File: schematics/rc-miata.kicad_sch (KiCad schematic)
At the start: 14 parts, among them M1 BLDC_MOTOR, M2 22KG SERVO, U2 UBEC, U3 ESC, U4 ESP32 DEVKITV1

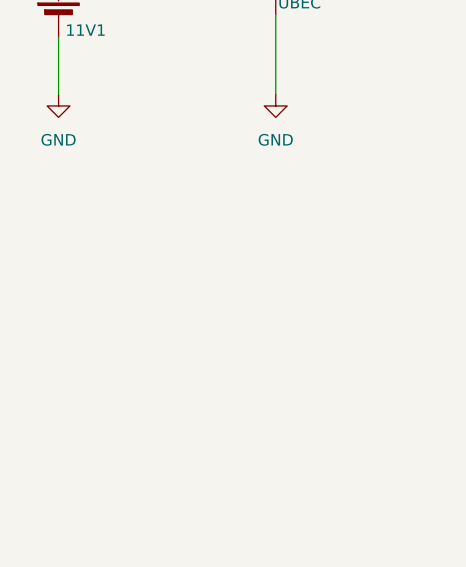
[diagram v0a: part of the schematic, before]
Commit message: Finished 2,3, and 4 Terminal Blocks Added Battery Terminal
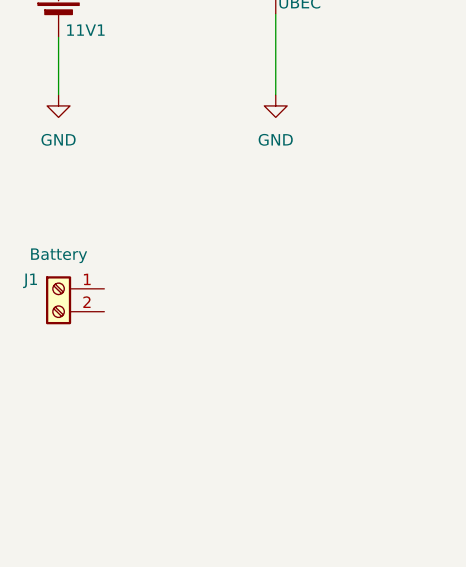
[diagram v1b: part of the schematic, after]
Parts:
- added J1: Battery, symbol Connectors:2 Screw Terminal
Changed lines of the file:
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@@
+	)
+	(symbol
+		(lib_id "Connectors:2 Screw Terminal")
+		(at 38.1 105.41 0)
+		(unit 1)
+		(body_style 1)
+		(exclude_from_sim no)
+		(in_bom yes)
+		(on_board yes)
+		(in_pos_files yes)
+		(dnp no)
+		(property "Reference" "J1"
+			(at 36.322 105.664 0)
+			(show_name no)
+			(do_not_autoplace no)
+			(effects
+				(font
+					(size 1.27 1.27)
+				)
+			)
+		)
+		(property "Value" "Battery"
+			(at 39.37 102.87 0)
+			(show_name no)
+			(do_not_autoplace no)
+			(effects
+				(font
+					(size 1.27 1.27)
+				)
+			)
+		)
+		(property "Footprint" ""
+			(at 38.1 105.41 0)
+			(hide yes)
+			(show_name no)
+			(do_not_autoplace no)
+			(effects
+				(font
+					(size 1.27 1.27)
+				)
+			)
+		)
+		(property "Datasheet" "https://www.mouser.ca/datasheet/3/507/9/phoenix_contact_1869211_en.pdf"
+			(at 59.944 127.508 0)
+			(hide yes)
+			(show_name no)
+			(do_not_autoplace no)
+			(effects
+				(font
+					(size 1.27 1.27)
+				)
+			)
+		)
+		(property "Description" "Phoenix Contact screw terminal, single row, 01x02"
+			(at 63.246 122.428 0)
+			(hide yes)
+			(show_name no)
+			(do_not_autoplace no)
+			(effects
+				(font
+					(size 1.27 1.27)
+				)
+			)
+		)
+		(property "Mfr. #" "1869211"
+			(at 42.418 119.888 0)
+			(hide yes)
+			(show_name no)
+			(do_not_autoplace no)
+			(effects
+				(font
+					(size 1.27 1.27)
+				)
+			)
+		)
+		(property "Mfr." "Phoenix Contact"
+			(at 46.228 124.46 0)
+			(hide yes)
+			(show_name no)
+			(do_not_autoplace no)
+			(effects
+				(font
+					(size 1.27 1.27)
+				)
+			)
+		)
+		(property "Mouser #" "651-1869211"
+			(at 45.72 130.556 0)
+			(hide yes)
+			(show_name no)
+			(do_not_autoplace no)
+			(effects
+				(font
+					(size 1.27 1.27)
+				)
+			)
+		)
+		(pin "1"
+		)
+		(pin "2"
+		)
+		(instances
+			(project "rc-miata"
+				(path "/59cbdaad-7c89-4958-b9bb-08b035442600"
+					(reference "J1")
+					(unit 1)
+				)
+			)
+		)
 	)
 	(symbol

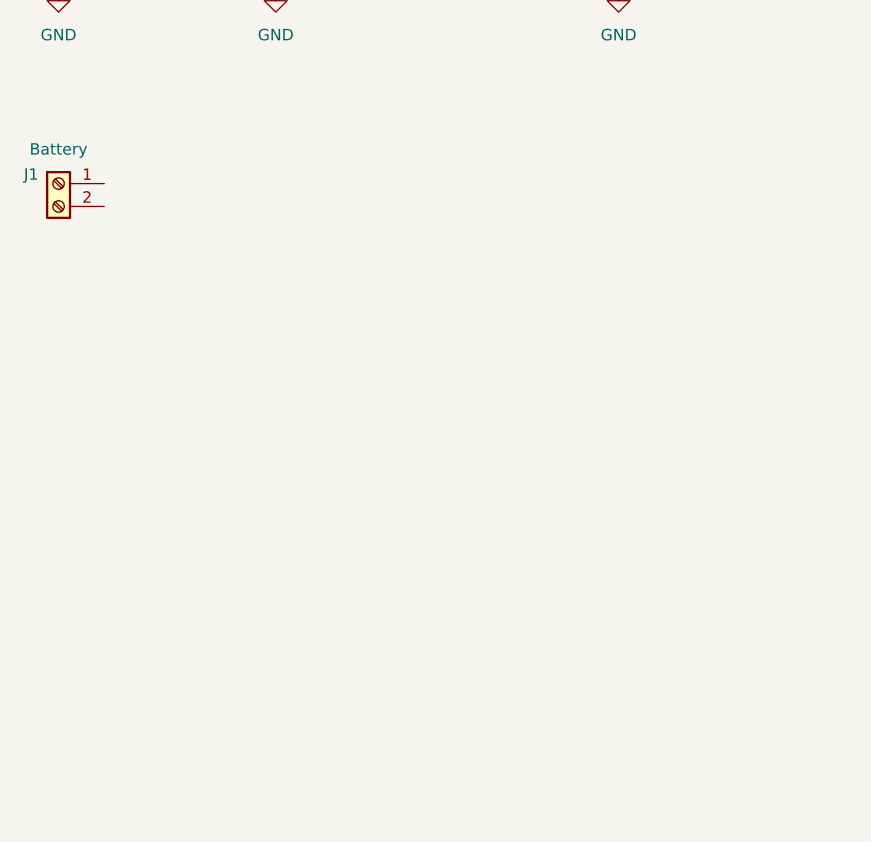
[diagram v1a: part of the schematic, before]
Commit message: Added and wired terminal blocks to schematic
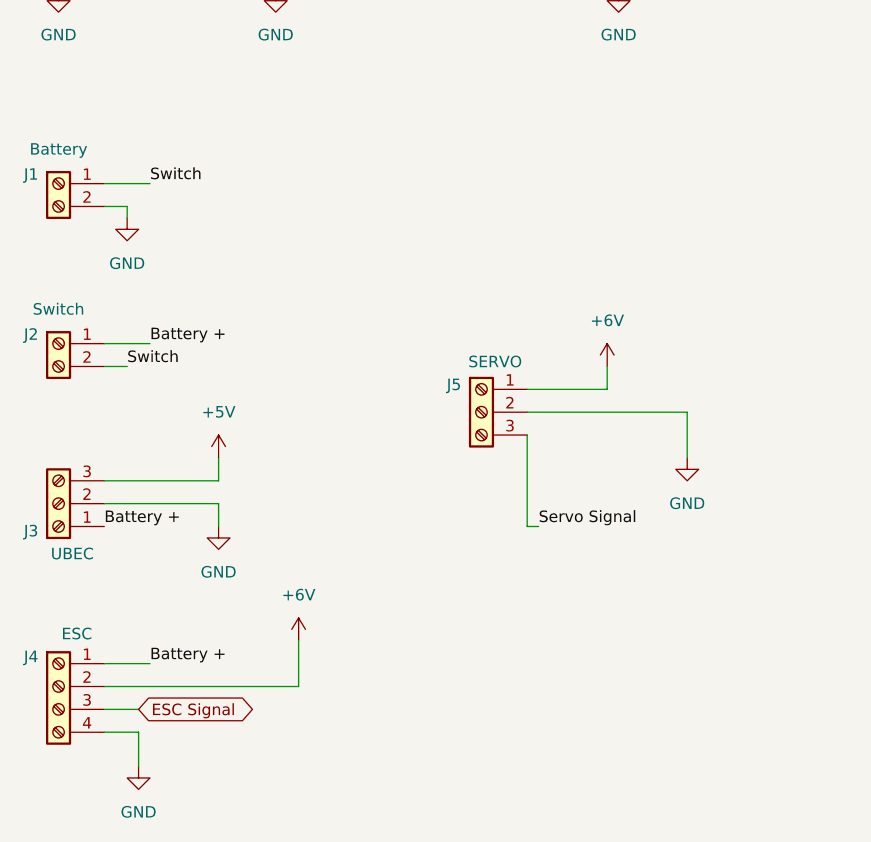
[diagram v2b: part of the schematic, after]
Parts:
- added J2: Switch, symbol Connectors:2 Screw Terminal
- added J3: UBEC, symbol Connectors:3 Screw Terminal
- added J4: ESC, symbol Connectors:4 Screw Terminal
- added J5: SERVO, symbol Connectors:3 Screw Terminal
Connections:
- net +5V: now also J3.3 (Pin_3)
- net +6V: now also J4.2 (Pin_2), J5.1 (Pin_1)
- net Battery +: now also J2.1 (Pin_1), J3.1 (Pin_1), J4.1 (Pin_1)
- net ESC Signal: now also J4.3 (Pin_3)
- net GND: now also J1.2 (Pin_2), J3.2 (Pin_2), J4.4 (Pin_4), J5.2 (Pin_2)
- net Servo Signal: now also J5.3 (Pin_3)
- net Switch: now also J1.1 (Pin_1), J2.2 (Pin_2)

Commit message: Fixed pin connections for servo and UBEC
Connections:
- net +5V: now also J3.1 (Pin_1); no longer J3.3 (Pin_3)
- net +6V: now also J5.3 (Pin_3); no longer J5.1 (Pin_1)
- net Battery +: now also J3.3 (Pin_3); no longer J3.1 (Pin_1)
- net Servo Signal: now also J5.1 (Pin_1); no longer J5.3 (Pin_3)
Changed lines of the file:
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@@
 	(symbol
 		(lib_id "Connectors:3 Screw Terminal")
-		(at 38.1 146.05 0)
-		(mirror x)
+		(at 38.1 138.43 0)
 		(unit 1)
 		(body_style 1)
@@
 		(dnp no)
 		(property "Reference" "J3"
-			(at 36.322 145.288 0)
+			(at 36.322 139.192 0)
 			(show_name no)
 			(do_not_autoplace no)
@@
 		)
 		(property "Value" "UBEC"
-			(at 40.894 147.828 0)
+			(at 40.894 136.652 0)
 			(show_name no)
 			(do_not_autoplace no)
@@
 		)
 		(property "Footprint" ""
-			(at 38.1 146.05 0)
+			(at 38.1 138.43 0)
 			(hide yes)
 			(show_name no)
@@
 		)
 		(property "Datasheet" "https://www.mouser.ca/datasheet/3/507/9/phoenix_contact_1161181_en.pdf"
-			(at 60.96 114.3 0)
+			(at 60.96 170.18 0)
 			(hide yes)
 			(show_name no)
@@
 		)
 		(property "Description" "Phoenix Contact screw terminal, single row, 01x03"
-			(at 63.246 129.032 0)
+			(at 63.246 155.448 0)
 			(hide yes)
 			(show_name no)
@@
 		)
 		(property "Mfr. #" "1161181"
-			(at 43.688 120.396 0)
+			(at 43.688 164.084 0)
 			(hide yes)
 			(show_name no)
@@
 		)
 		(property "Mfr." "Phoenix Contact"
-			(at 46.228 127 0)
+			(at 46.228 157.48 0)
 			(hide yes)
 			(show_name no)
@@
 		)
 		(property "Mouser #" "651-1161181"
-			(at 45.212 117.348 0)
+			(at 45.212 167.132 0)
 			(hide yes)
 			(show_name no)
@@
 		)
 		(property "Seller" "https://www.mouser.ca/ProductDetail/Phoenix-Contact/1161181?qs=sGAEpiMZZMvPvGwLNS671%252B7aWYNAXBhXqhzIwd5MSQGBxEXmvvVG1Q%3D%3D"
-			(at 60.452 110.744 0)
+			(at 60.452 173.736 0)
 			(hide yes)
 			(show_name no)
@@
 	(symbol
 		(lib_id "Connectors:3 Screw Terminal")
-		(at 85.09 128.27 0)
+		(at 85.09 135.89 0)
+		(mirror x)
 		(unit 1)
 		(body_style 1)
@@
 		(dnp no)
 		(property "Reference" "J5"
-			(at 83.312 129.032 0)
+			(at 83.312 135.128 0)
 			(show_name no)
 			(do_not_autoplace no)
@@
 		)
 		(property "Value" "SERVO"
-			(at 87.884 126.492 0)
+			(at 87.884 137.668 0)
 			(show_name no)
 			(do_not_autoplace no)
@@
 		)
 		(property "Footprint" ""
-			(at 85.09 128.27 0)
+			(at 85.09 135.89 0)
 			(hide yes)
 			(show_name no)
@@
 		)
 		(property "Datasheet" "https://www.mouser.ca/datasheet/3/507/9/phoenix_contact_1161181_en.pdf"
-			(at 107.95 160.02 0)
+			(at 107.95 104.14 0)
 			(hide yes)
 			(show_name no)
@@
 		)
 		(property "Description" "Phoenix Contact screw terminal, single row, 01x03"
-			(at 110.236 145.288 0)
+			(at 110.236 118.872 0)
 			(hide yes)
 			(show_name no)
@@
 		)
 		(property "Mfr. #" "1161181"
-			(at 90.678 153.924 0)
+			(at 90.678 110.236 0)
 			(hide yes)
 			(show_name no)
@@
 		)
 		(property "Mfr." "Phoenix Contact"
-			(at 93.218 147.32 0)
+			(at 93.218 116.84 0)
 			(hide yes)
 			(show_name no)
@@
 		)
 		(property "Mouser #" "651-1161181"
-			(at 92.202 156.972 0)
+			(at 92.202 107.188 0)
 			(hide yes)
 			(show_name no)
@@
 		)
 		(property "Seller" "https://www.mouser.ca/ProductDetail/Phoenix-Contact/1161181?qs=sGAEpiMZZMvPvGwLNS671%252B7aWYNAXBhXqhzIwd5MSQGBxEXmvvVG1Q%3D%3D"
-			(at 107.442 163.576 0)
+			(at 107.442 100.584 0)
 			(hide yes)
 			(show_name no)

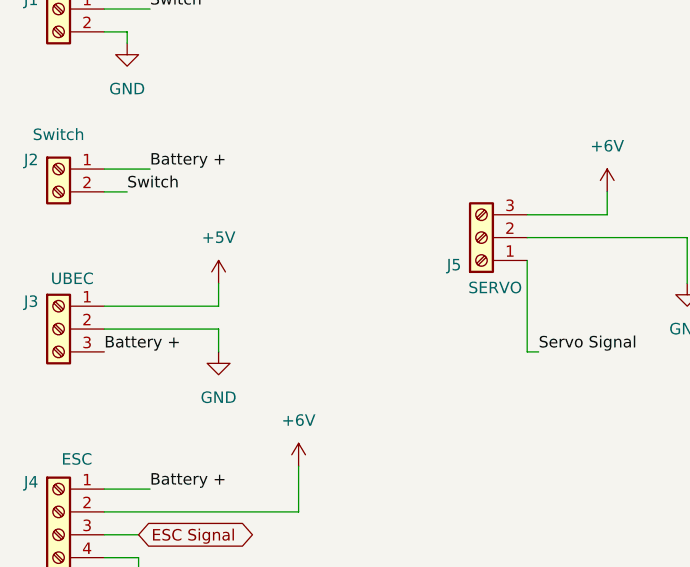
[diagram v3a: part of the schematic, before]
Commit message: Applied footprints
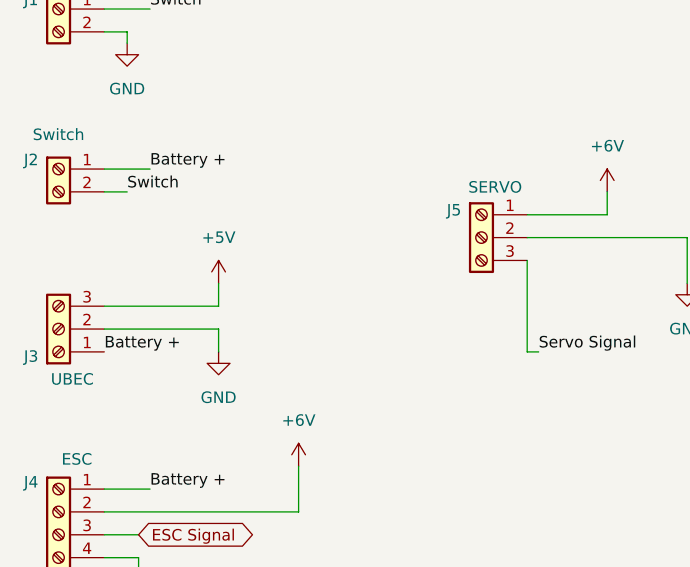
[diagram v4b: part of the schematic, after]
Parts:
- D1, D2, D3, D4: footprint (none) -> LED_THT:LED_D3.0mm
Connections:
- net +5V: now also J3.3 (Pin_3); no longer J3.1 (Pin_1)
- net +6V: now also J5.1 (Pin_1); no longer J5.3 (Pin_3)
- net Battery +: now also J3.1 (Pin_1); no longer J3.3 (Pin_3)
- net Servo Signal: now also J5.3 (Pin_3); no longer J5.1 (Pin_1)
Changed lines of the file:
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@@
 	(wire
 		(pts
+			(xy 91.44 134.62) (xy 91.44 144.78)
+		)
+		(stroke
+			(width 0)
+			(type default)
+		)
+	)
+	(wire
+		(pts
 			(xy 91.44 66.04) (xy 88.9 66.04)
 		)
@@
 	(wire
 		(pts
-			(xy 91.44 134.62) (xy 91.44 144.78)
-		)
-		(stroke
-			(width 0)
-			(type default)
-		)
-	)
-	(wire
-		(pts
 			(xy 111.76 71.12) (xy 116.84 71.12)
 		)
@@
 	(symbol
 		(lib_id "Connectors:3 Screw Terminal")
-		(at 38.1 138.43 0)
+		(at 38.1 146.05 0)
+		(mirror x)
 		(unit 1)
 		(body_style 1)
@@
 		(dnp no)
 		(property "Reference" "J3"
-			(at 36.322 139.192 0)
+			(at 36.322 145.288 0)
 			(show_name no)
 			(do_not_autoplace no)
@@
 		)
 		(property "Value" "UBEC"
-			(at 40.894 136.652 0)
+			(at 40.894 147.828 0)
 			(show_name no)
 			(do_not_autoplace no)
@@
 		)
 		(property "Footprint" ""
-			(at 38.1 138.43 0)
+			(at 38.1 146.05 0)
 			(hide yes)
 			(show_name no)
@@
 		)
 		(property "Datasheet" "https://www.mouser.ca/datasheet/3/507/9/phoenix_contact_1161181_en.pdf"
-			(at 60.96 170.18 0)
+			(at 60.96 114.3 0)
 			(hide yes)
 			(show_name no)
@@
 		)
 		(property "Description" "Phoenix Contact screw terminal, single row, 01x03"
-			(at 63.246 155.448 0)
+			(at 63.246 129.032 0)
 			(hide yes)
 			(show_name no)
@@
 		)
 		(property "Mfr. #" "1161181"
-			(at 43.688 164.084 0)
+			(at 43.688 120.396 0)
 			(hide yes)
 			(show_name no)
@@
 		)
 		(property "Mfr." "Phoenix Contact"
-			(at 46.228 157.48 0)
+			(at 46.228 127 0)
 			(hide yes)
 			(show_name no)
@@
 		)
 		(property "Mouser #" "651-1161181"
-			(at 45.212 167.132 0)
+			(at 45.212 117.348 0)
 			(hide yes)
 			(show_name no)
@@
 		)
 		(property "Seller" "https://www.mouser.ca/ProductDetail/Phoenix-Contact/1161181?qs=sGAEpiMZZMvPvGwLNS671%252B7aWYNAXBhXqhzIwd5MSQGBxEXmvvVG1Q%3D%3D"
-			(at 60.452 173.736 0)
+			(at 60.452 110.744 0)
 			(hide yes)
 			(show_name no)
@@
 			)
 		)
-		(property "Footprint" ""
+		(property "Footprint" "LED_THT:LED_D3.0mm"
 			(at 233.68 135.89 0)
 			(hide yes)
@@
 			)
 		)
-		(property "Footprint" ""
+		(property "Footprint" "LED_THT:LED_D3.0mm"
 			(at 233.68 143.51 0)
 			(hide yes)
@@
 			)
 		)
-		(property "Footprint" ""
+		(property "Footprint" "LED_THT:LED_D3.0mm"
 			(at 233.68 151.13 0)
 			(hide yes)
@@
 			)
 		)
-		(property "Footprint" ""
+		(property "Footprint" "LED_THT:LED_D3.0mm"
 			(at 233.68 128.27 0)
 			(hide yes)
@@
 	(symbol
 		(lib_id "Connectors:3 Screw Terminal")
-		(at 85.09 135.89 0)
-		(mirror x)
+		(at 85.09 128.27 0)
 		(unit 1)
 		(body_style 1)
@@
 		(dnp no)
 		(property "Reference" "J5"
-			(at 83.312 135.128 0)
+			(at 83.312 129.032 0)
 			(show_name no)
 			(do_not_autoplace no)
@@
 		)
 		(property "Value" "SERVO"
-			(at 87.884 137.668 0)
+			(at 87.884 126.492 0)
 			(show_name no)
 			(do_not_autoplace no)
@@
 		)
 		(property "Footprint" ""
-			(at 85.09 135.89 0)
+			(at 85.09 128.27 0)
 			(hide yes)
 			(show_name no)
@@
 		)
 		(property "Datasheet" "https://www.mouser.ca/datasheet/3/507/9/phoenix_contact_1161181_en.pdf"
-			(at 107.95 104.14 0)
+			(at 107.95 160.02 0)
 			(hide yes)
 			(show_name no)
@@
 		)
 		(property "Description" "Phoenix Contact screw terminal, single row, 01x03"
-			(at 110.236 118.872 0)
+			(at 110.236 145.288 0)
 			(hide yes)
 			(show_name no)
@@
 		)
 		(property "Mfr. #" "1161181"
-			(at 90.678 110.236 0)
+			(at 90.678 153.924 0)
 			(hide yes)
 			(show_name no)
@@
 		)
 		(property "Mfr." "Phoenix Contact"
-			(at 93.218 116.84 0)
+			(at 93.218 147.32 0)
 			(hide yes)
 			(show_name no)
@@
 		)
 		(property "Mouser #" "651-1161181"
-			(at 92.202 107.188 0)
+			(at 92.202 156.972 0)
 			(hide yes)
 			(show_name no)
@@
 		)
 		(property "Seller" "https://www.mouser.ca/ProductDetail/Phoenix-Contact/1161181?qs=sGAEpiMZZMvPvGwLNS671%252B7aWYNAXBhXqhzIwd5MSQGBxEXmvvVG1Q%3D%3D"
-			(at 107.442 100.584 0)
+			(at 107.442 163.576 0)
 			(hide yes)
 			(show_name no)

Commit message: Updated header blocks. Populated PCB title block
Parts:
- J1, J2: footprint (none) -> Connectors:1869211; Seller (none) -> https://www.mouser.ca/ProductDetail/Phoenix-Contact/1869211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
- J3, J5: footprint (none) -> Connectors:1161181
- J4: footprint (none) -> Connectors:1869237; Seller (none) -> https://www.mouser.ca/ProductDetail/Phoenix-Contact/1869237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
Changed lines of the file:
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@@
 			)
 		)
-		(property "Footprint" ""
+		(property "Footprint" "Connectors:1161181"
 			(at 38.1 146.05 0)
 			(hide yes)
@@
 			)
 		)
-		(property "Footprint" ""
+		(property "Footprint" "Connectors:1869211"
 			(at 38.1 123.19 0)
 			(hide yes)
@@
 		(property "Mouser #" "651-1869211"
 			(at 45.72 148.336 0)
+			(hide yes)
+			(show_name no)
+			(do_not_autoplace no)
+			(effects
+				(font
+					(size 1.27 1.27)
+				)
+			)
+		)
+		(property "Seller" "https://www.mouser.ca/ProductDetail/Phoenix-Contact/1869211?qs=8M15sSGRUn9uIaAw90nKPw%3D%3D"
+			(at 66.294 153.924 0)
 			(hide yes)
 			(show_name no)
@@
 			)
 		)
-		(property "Footprint" ""
+		(property "Footprint" "Connectors:1869237"
 			(at 38.1 158.75 0)
 			(hide yes)
@@
 			)
 		)
+		(property "Seller" "https://www.mouser.ca/ProductDetail/Phoenix-Contact/1869237?qs=8M15sSGRUn9rCp2zUK%2Fgyw%3D%3D"
+			(at 59.182 187.706 0)
+			(hide yes)
+			(show_name no)
+			(do_not_autoplace no)
+			(effects
+				(font
+					(size 1.27 1.27)
+				)
+			)
+		)
 		(pin "4"
 		)
@@
 	)
 	(symbol
+		(lib_name "2 Screw Terminal_1")
 		(lib_id "Connectors:2 Screw Terminal")
 		(at 38.1 105.41 0)
@@
 			)
 		)
-		(property "Footprint" ""
+		(property "Footprint" "Connectors:1869211"
 			(at 38.1 105.41 0)
 			(hide yes)
@@
 		(property "Mouser #" "651-1869211"
 			(at 45.72 130.556 0)
+			(hide yes)
+			(show_name no)
+			(do_not_autoplace no)
+			(effects
+				(font
+					(size 1.27 1.27)
+				)
+			)
+		)
+		(property "Seller" "https://www.mouser.ca/ProductDetail/Phoenix-Contact/1869211?qs=8M15sSGRUn9uIaAw90nKPw%3D%3D"
+			(at 38.1 105.41 0)
 			(hide yes)
 			(show_name no)
@@
 		(exclude_from_sim no)
 		(in_bom yes)
-		(on_board yes)
+		(on_board no)
 		(in_pos_files yes)
 		(dnp no)
@@
 			)
 		)
-		(property "Footprint" ""
+		(property "Footprint" "Connectors:1161181"
 			(at 85.09 128.27 0)
 			(hide yes)
